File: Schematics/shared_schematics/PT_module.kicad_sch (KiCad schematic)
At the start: 5 parts, among them J4 PT1

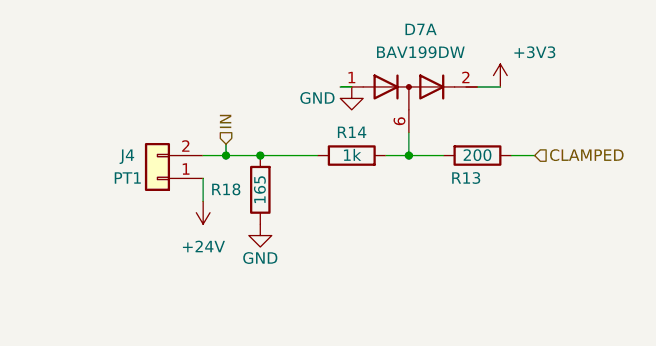
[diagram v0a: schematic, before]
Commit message: add references to caps, ferrite bead footprint, LDO datasheet
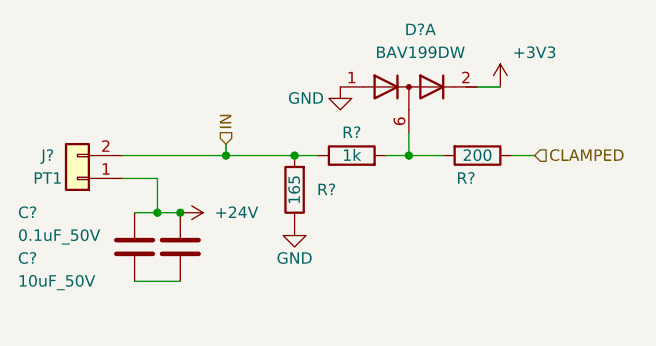
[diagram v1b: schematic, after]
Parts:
- removed R13: 200, Resistor_SMD:R_0603_1608Metric, symbol Device:R
- removed R14: 1k, Resistor_SMD:R_1206_3216Metric_Pad1.30x1.75mm_HandSolder, symbol Device:R
- added C?: 0.1uF_50V, Capacitor_SMD:C_0805_2012Metric, symbol Device:C
- added C?: 10uF_50V, Capacitor_SMD:C_1206_3216Metric, symbol Device:C
- added R?: 200, Resistor_SMD:R_0603_1608Metric, symbol Device:R
- added R?: 1k, Resistor_SMD:R_1206_3216Metric_Pad1.30x1.75mm_HandSolder, symbol Device:R
- renumbered D7 to D?, J4 to J?, R18 to R?
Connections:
- net +24V: now also C?.1, C?.1
- net CLAMPED: now also R?.1
- net IN: now also R?.1
- net at D?.6 (K3A4): now also R?.2, R?.2
- new net: C?.2, C?.2
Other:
- moved on the sheet: J?, R?

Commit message: add decoupling, revise power circuitry (ferrite bead, LDO swap), merge shared-schemtic branch changes.
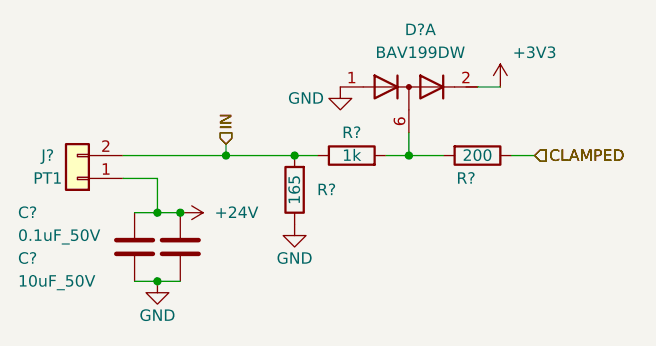
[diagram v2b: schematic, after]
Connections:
- net GND: now also C?.2, C?.2
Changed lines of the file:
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@@
+	)
+	(junction
+		(at 113.03 109.22)
+		(diameter 0)
+		(color 0 0 0 0)
 	)
 	(junction
@@
 	(wire
 		(pts
-			(xy 110.49 109.22) (xy 115.57 109.22)
+			(xy 110.49 109.22) (xy 113.03 109.22)
 		)
 		(stroke
@@
 		(pts
 			(xy 138.43 95.25) (xy 140.97 95.25)
+		)
+		(stroke
+			(width 0)
+			(type default)
+		)
+	)
+	(wire
+		(pts
+			(xy 113.03 109.22) (xy 115.57 109.22)
 		)
 		(stroke
@@
 		(shape input)
 		(at 120.65 93.98 90)
+		(fields_autoplaced yes)
+		(effects
+			(font
+				(size 1.27 1.27)
+			)
+			(justify left)
+		)
+	)
+	(hierarchical_label "IN"
+		(shape input)
+		(at 120.65 93.98 90)
+		(fields_autoplaced yes)
+		(effects
+			(font
+				(size 1.27 1.27)
+			)
+			(justify left)
+		)
+	)
+	(hierarchical_label "CLAMPED"
+		(shape input)
+		(at 154.94 95.25 0)
 		(fields_autoplaced yes)
 		(effects
@@
 				(path "/9b1a1d2a-fad7-4f10-83f3-1f83e9656c75/03f1622b-3dda-4e29-911f-7cc762ec6c20/3fcdaac5-2869-40f8-b925-cf310375456d"
 					(reference "J3")
+					(unit 1)
+				)
+			)
+		)
+	)
+	(symbol
+		(lib_id "power:GND")
+		(at 113.03 109.22 0)
+		(unit 1)
+		(exclude_from_sim no)
+		(in_bom yes)
+		(on_board yes)
+		(dnp no)
+		(property "Reference" "#PWR042"
+			(at 113.03 115.57 0)
+			(effects
+				(font
+					(size 1.27 1.27)
+				)
+				(hide yes)
+			)
+		)
+		(property "Value" "GND"
+			(at 113.03 113.03 0)
+			(effects
+				(font
+					(size 1.27 1.27)
+				)
+			)
+		)
+		(property "Footprint" ""
+			(at 113.03 109.22 0)
+			(effects
+				(font
+					(size 1.27 1.27)
+				)
+				(hide yes)
+			)
+		)
+		(property "Datasheet" "https://www.ti.com/lit/ds/symlink/drv5055.pdf?HQS=dis-dk-null-digikeymode-dsf-pf-null-wwe&ts=1641231273160"
+			(at 113.03 109.22 0)
+			(effects
+				(font
+					(size 1.27 1.27)
+				)
+				(hide yes)
+			)
+		)
+		(property "Description" "Hall effect sensor."
+			(at 113.03 109.22 0)
+			(effects
+				(font
+					(size 1.27 1.27)
+				)
+				(hide yes)
+			)
+		)
+		(pin "1"
+		)
+		(instances
+			(project "upper_lc_board"
+				(path "/9b1a1d2a-fad7-4f10-83f3-1f83e9656c75/03f1622b-3dda-4e29-911f-7cc762ec6c20/053ff26d-da11-4577-8dd0-32aaebff2a7b"
+					(reference "#PWR042")
+					(unit 1)
+				)
+				(path "/9b1a1d2a-fad7-4f10-83f3-1f83e9656c75/03f1622b-3dda-4e29-911f-7cc762ec6c20/3fcdaac5-2869-40f8-b925-cf310375456d"
+					(reference "#PWR043")
 					(unit 1)
 				)
@@
 		)
 	)
-	(sheet_instances
-		(path "/"
-			(page "1")
-		)
-	)
